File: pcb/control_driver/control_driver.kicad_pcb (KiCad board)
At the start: 2 copper layers, 99.1 x 74.9 mm, 64 parts, among them P1 CONN_2, P2 CONN_4, P3 CONN_2, P4 CONN_4, P5 CONN_4, P6 CONN_4, P7 CONN_4, Q1 MOSFET_N, Q2 MOSFET_N, Q3 MOSFET_N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

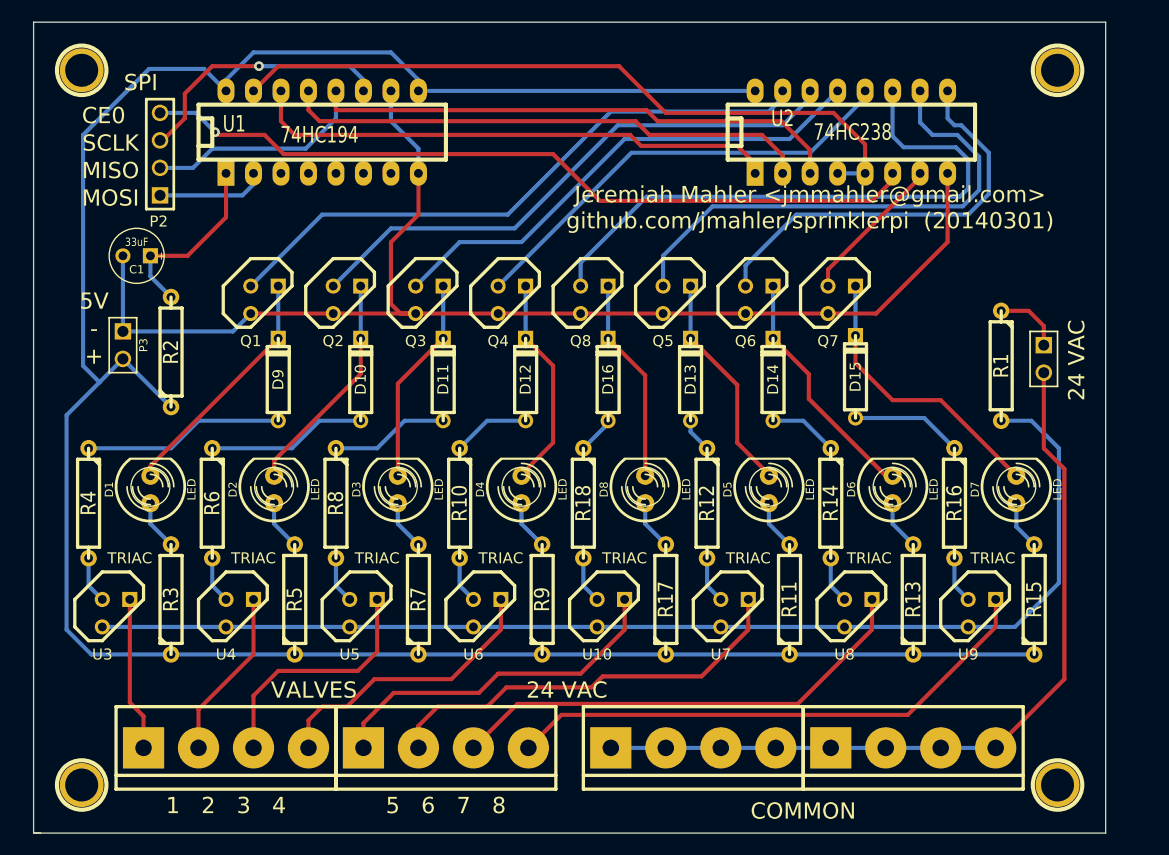
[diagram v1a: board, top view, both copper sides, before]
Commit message: control PCB connectors now on left side
The input connectors for the control PCB have been
moved to the left side of the board.  This should
help reduce the wire length required to connect
between boards.
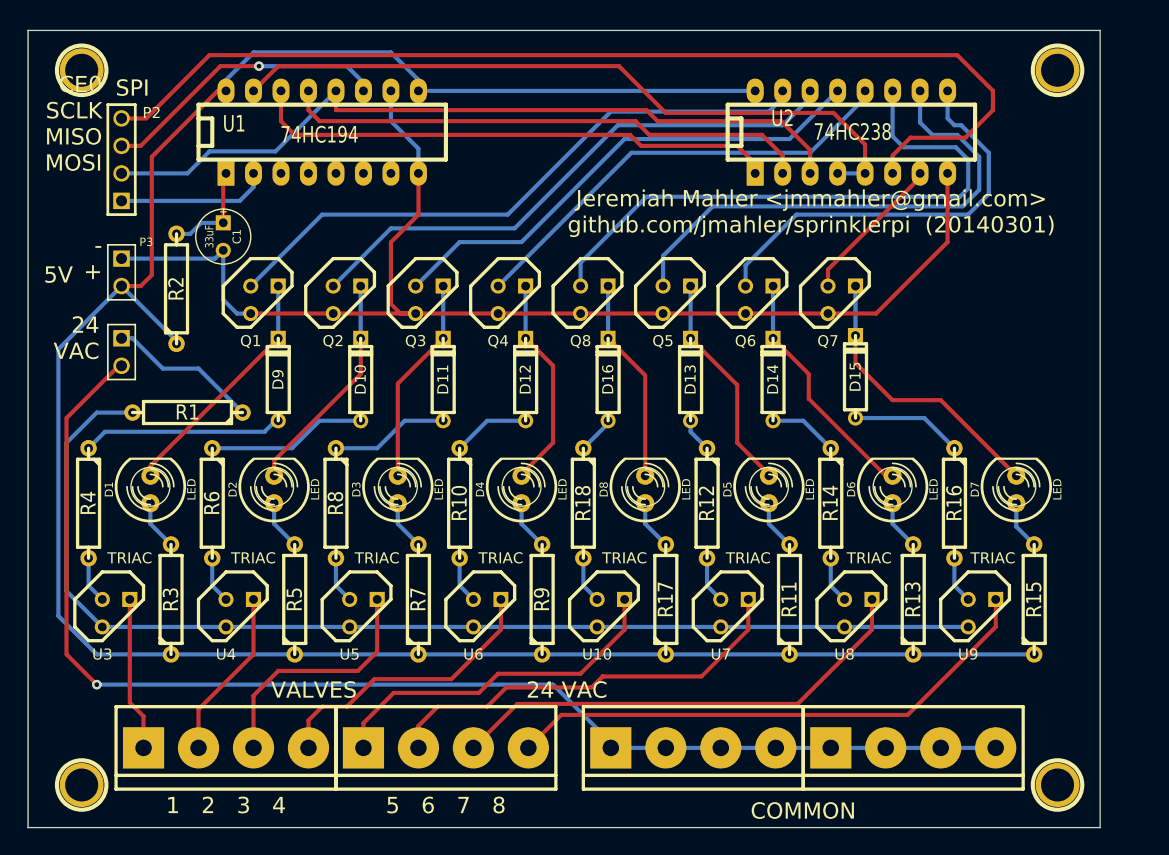
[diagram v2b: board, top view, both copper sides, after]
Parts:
- moved P1 85.2 mm to (178.3, 166.4)
- moved R1 75.3 mm to (184.4, 172.0), turned to 180 degrees
- moved C1 8.20 mm to (187.7, 155.7), turned to 270 degrees
- moved P3 6.73 mm to (178.3, 159.0)
- moved R2 5.86 mm to (183.4, 160.5)
- moved P2 3.59 mm to (178.3, 148.6)
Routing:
- net N-0000015: track 73.7 -> 118.6 mm, vias 0 -> 1
- net /control/CE0: track 72.5 -> 98.7 mm, vias 1 -> 0
- net +5V: track 216.3 -> 207.9 mm
- net N-000001: track 6.29 -> 14.0 mm
- net N-0000031: track 17.1 -> 9.42 mm
- net /control/MOSI: track 10.1 -> 14.0 mm
- net /driver_1/DRV_A: track 108.9 -> 105.6 mm
- net /control/MISO: track 70.0 -> 72.2 mm
- net /control/SCLK: track 24.5 -> 26.8 mm
- net GND: track 117.4 -> 115.3 mm
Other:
- board size 99.1 x 74.9 mm -> 99.1 x 73.7 mm
- board text added: "- +"
- board text added: "CE0 SCLK MISO MOSI"
- board text removed: "+"
- board text removed: "-"
- board text removed: "CE0"
- board text removed: "MISO"
- board text removed: "MOSI"
- board text removed: "SCLK"

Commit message: refactored control_driver PCB (3.9" x 2.76")
Refactored control_driver PCB.  Got size down to 3.9" x 2.76".
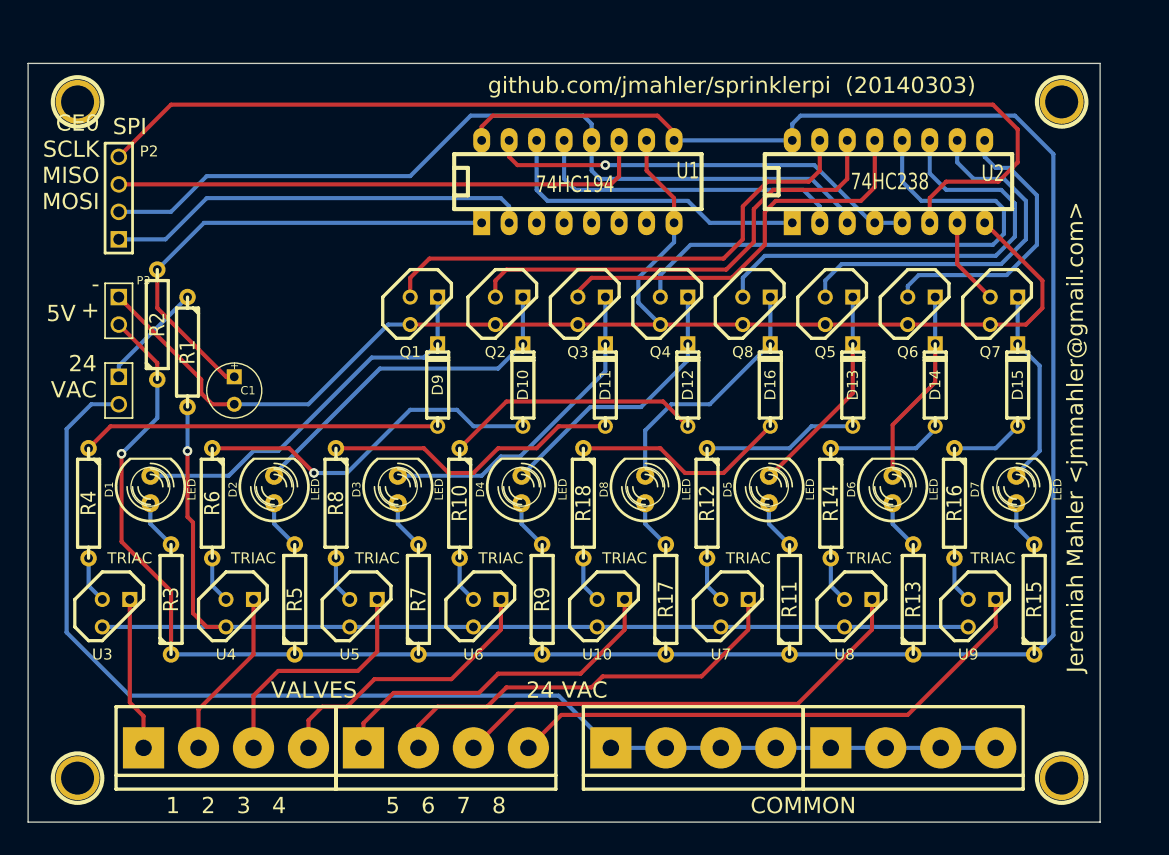
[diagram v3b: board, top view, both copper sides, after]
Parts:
- moved U1 24.1 mm to (220.5, 150.6)
- moved Q2 15.0 mm to (214.1, 162.6)
- moved Q6 15.0 mm to (252.2, 162.6)
- moved Q3 15.0 mm to (221.7, 162.6)
- moved Q4 15.0 mm to (229.4, 162.6)
- moved Q5 15.0 mm to (244.6, 162.6)
- moved Q7 15.0 mm to (259.8, 162.6)
- moved Q8 15.0 mm to (237.0, 162.6)
- moved D15 15.0 mm to (261.1, 169.4)
- moved D12 15.0 mm to (230.6, 169.4)
- moved D13 15.0 mm to (245.9, 169.4)
- moved D16 15.0 mm to (238.3, 169.4)
- moved D10 15.0 mm to (215.4, 169.4)
- moved D11 15.0 mm to (223.0, 169.4)
- moved D14 15.0 mm to (253.5, 169.4)
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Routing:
- net N-0000031: track 9.42 -> 45.1 mm
- net /control/MOSI: track 14.0 -> 39.5 mm
- net N-0000034: track 65.7 -> 40.4 mm, vias 0 -> 1
- net /control/SCLK: track 26.8 -> 49.8 mm, vias 1 -> 0
- net N-0000033: track 49.1 -> 29.5 mm
- net N-0000032: track 49.0 -> 29.8 mm
- net N-0000040: track 14.8 -> 32.7 mm, vias 0 -> 1
- net N-0000047: track 7.15 -> 23.8 mm
- net N-0000045: track 11.0 -> 27.6 mm
- net N-0000057: track 3.49 -> 20.0 mm
- net N-0000053: track 18.6 -> 33.1 mm
- net N-0000052: track 22.4 -> 35.9 mm
- net +5V: track 207.9 -> 220.5 mm, vias 0 -> 1
- net /driver_6/CTL: track 47.3 -> 35.1 mm
- net /driver_5/CTL: track 55.6 -> 43.6 mm
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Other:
- board size 99.1 x 73.7 mm -> 99.1 x 70.1 mm
- board text added: "Jeremiah Mahler <jmmahler@gmail.com>"
- board text added: "github.com/jmahler/sprinklerpi (20140303)"
- board text removed: "Jeremiah Mahler <jmmahler@gmail.com> github.com/jmahler/sprinklerpi (20140301)"

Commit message: updated control_driver PCB date
Updated the date on the control_driver PCB to match
the power24 PCB.
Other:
- board text added: "github.com/jmahler/sprinklerpi (20140304)"
- board text removed: "github.com/jmahler/sprinklerpi (20140303)"
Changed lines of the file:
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@@
   (gr_line (start 169.672 209.804) (end 268.732 209.804) (angle 90) (layer Edge.Cuts) (width 0.1))
   (gr_line (start 169.672 139.7) (end 169.672 209.804) (angle 90) (layer Edge.Cuts) (width 0.1))
-  (gr_text "github.com/jmahler/sprinklerpi  (20140303)" (at 234.696 141.732) (layer F.SilkS)
+  (gr_text "github.com/jmahler/sprinklerpi  (20140304)" (at 234.696 141.732) (layer F.SilkS)
     (effects (font (size 1.5 1.5) (thickness 0.3)))
   )
